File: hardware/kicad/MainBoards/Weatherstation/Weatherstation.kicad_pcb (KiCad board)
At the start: 2 copper layers, 113 x 93 mm, 37 parts, among them J1 Conn_02x07_Odd_Even, U1 ORingPower_Module, U2 24LC32, U3 ESP32-DevKitC

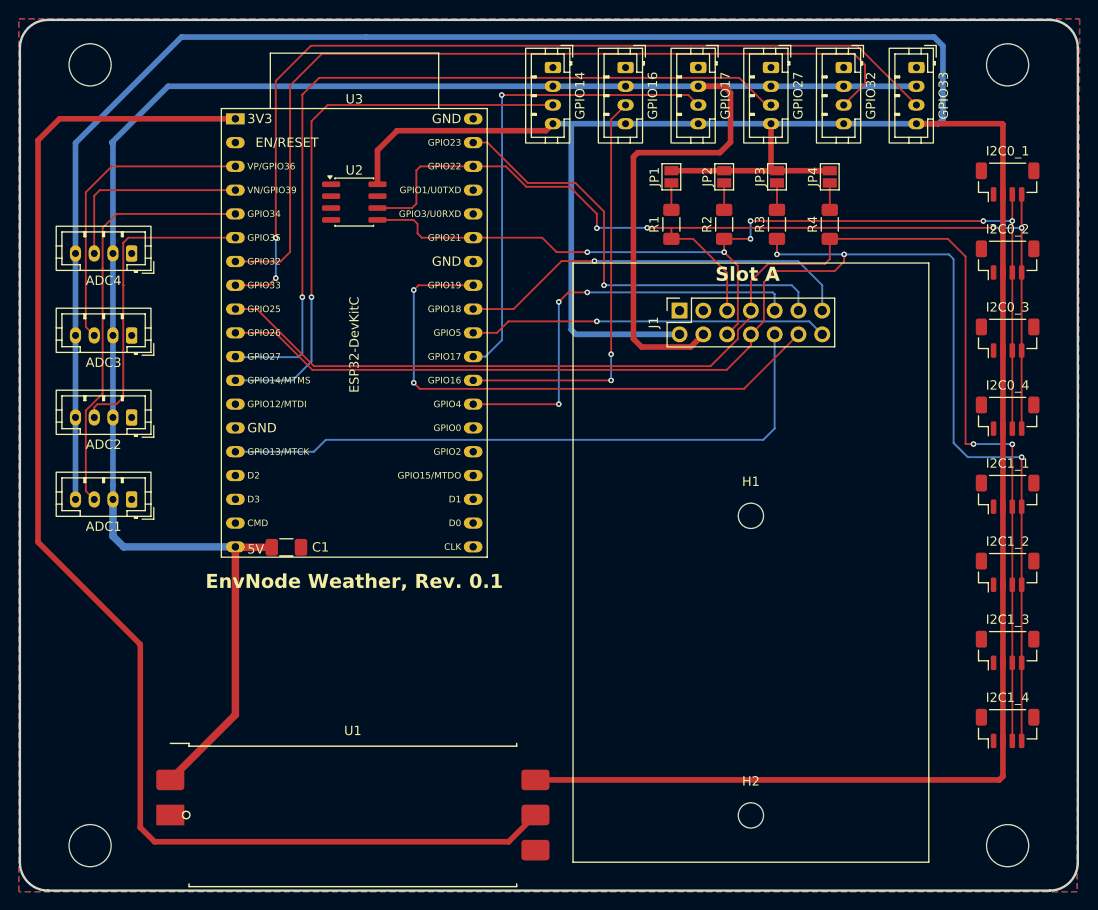
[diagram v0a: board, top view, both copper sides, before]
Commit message: hardware(weather): swap slot GPIO4 with GPIO33 for analog input
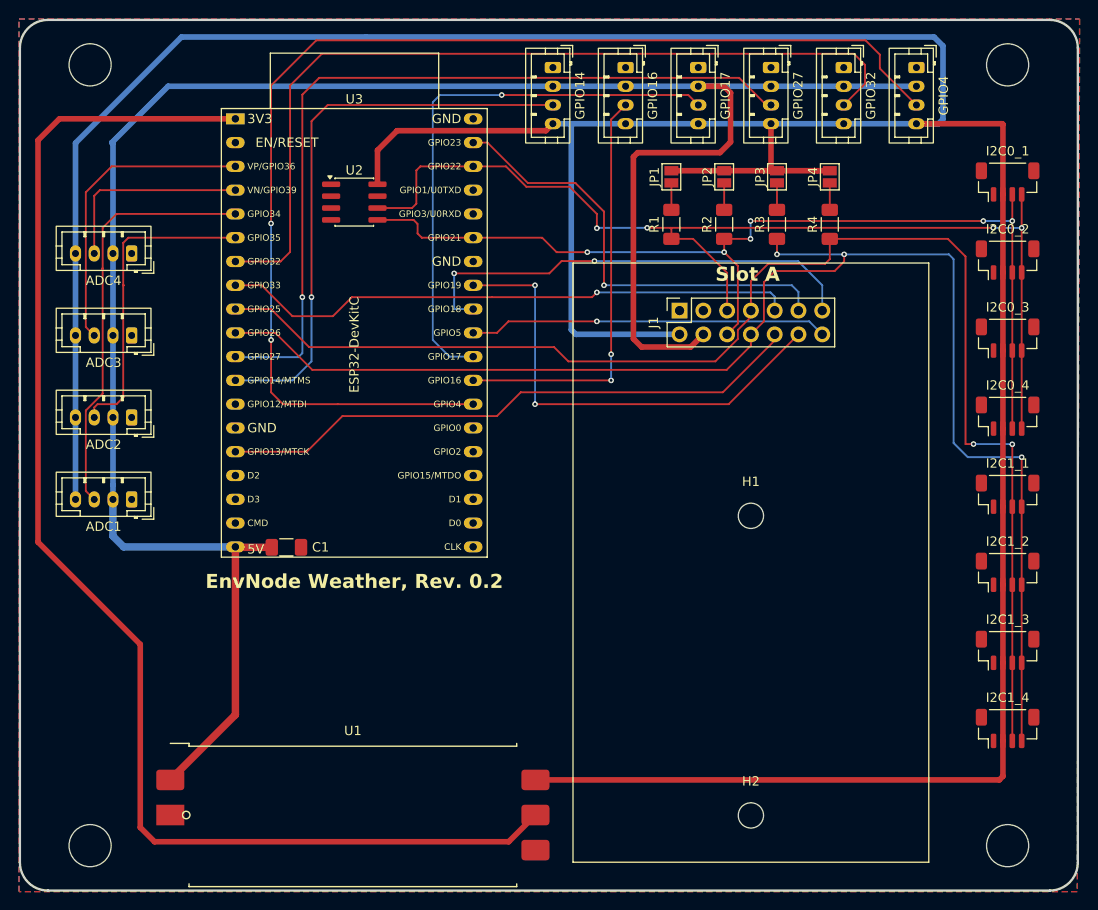
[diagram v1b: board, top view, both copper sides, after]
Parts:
- renumbered GPIO33 to GPIO4
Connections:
- GPIO4 pad 3: GPIO33 -> GPIO4
- J1 pad 9: GPIO4 -> GPIO33
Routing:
- net GPIO4: track 45.9 -> 129.5 mm, vias 3 -> 2
- net GPIO33: track 98.3 -> 62.2 mm, vias 2 -> 1
- net MISO: track 60.7 -> 51.0 mm
- net GPIO17: track 51.4 -> 59.6 mm
- net SCK: track 43.2 -> 49.5 mm, vias 1 -> 2
- net GPIO13: track 68.7 -> 63.2 mm

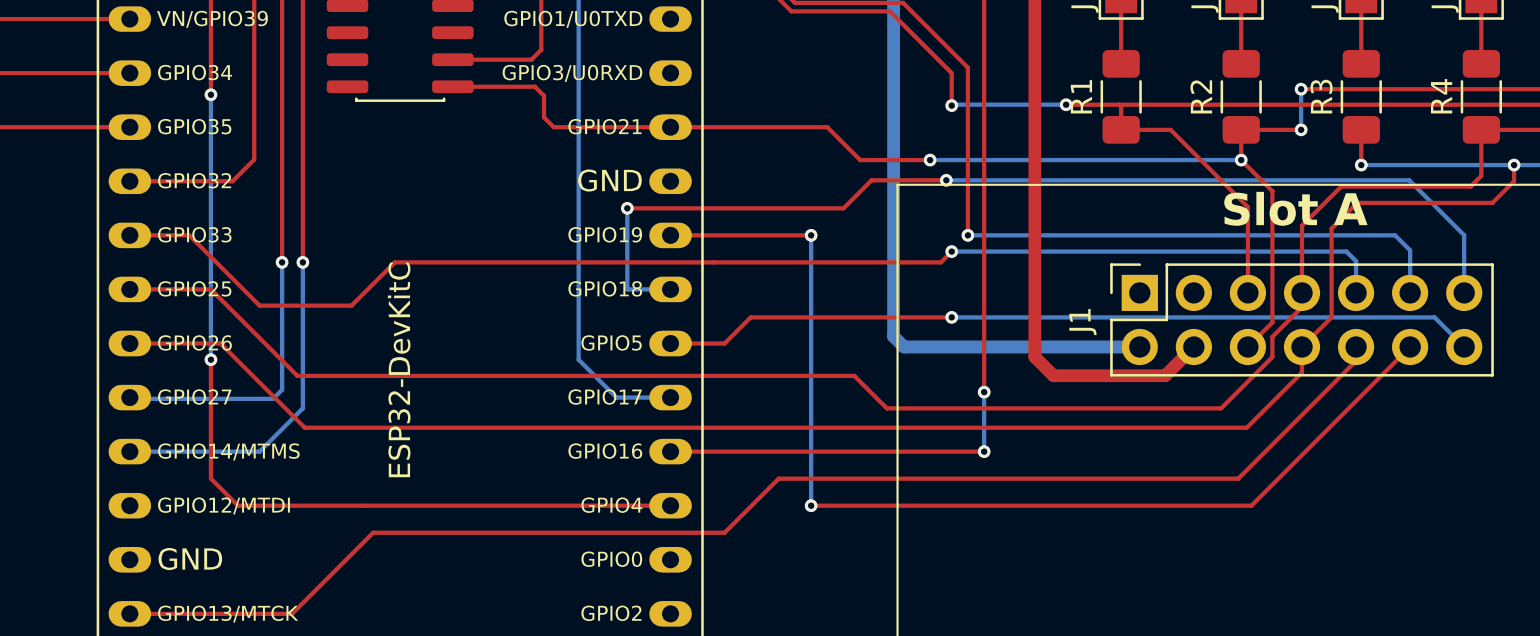
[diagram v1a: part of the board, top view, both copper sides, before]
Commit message: hardware(weather): finalize revision 0.2 with corrected module I2C0 pinout
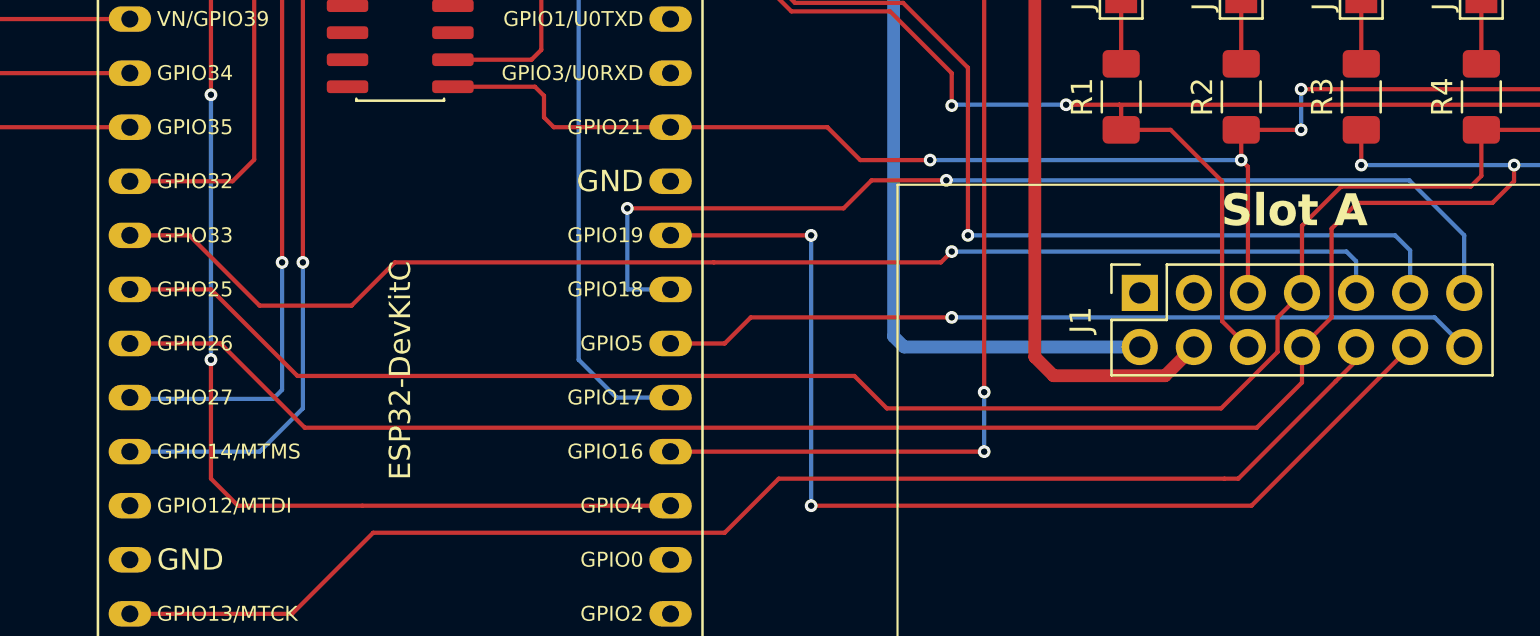
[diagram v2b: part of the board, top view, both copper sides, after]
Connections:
- J1 pad 5: I2C0_SCL -> I2C0_SDA
- J1 pad 6: I2C0_SDA -> I2C0_SCL
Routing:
- net I2C0_SDA: track 108.3 -> 104.8 mm
- net I2C0_SCL: track 114.1 -> 116.7 mm

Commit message: Document connector references and compatible PCB silkscreen revisions
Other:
- board text added: "GND +5V GPIO 3.3V"
- board text added: "GND 3V3 SDA0 SCL0"
- board text added: "GND 3V3 SDA1 SCL1"
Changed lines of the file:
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@@
 	(title_block
 		(title "EnvNode Weather")
-		(date "2026-09-28")
-		(rev "0.2")
+		(date "2026-10-18")
+		(rev "0.2.1")
 	)
 	(layers
@@
 	)
 	(footprint "Connector_JST:JST_PH_B4B-PH-K_1x04_P2.00mm_Vertical"
+		(locked yes)
 		(layer "F.Cu")
 		(at 68.17 101.35925 180)
@@
 	)
 	(footprint "Connector_JST:JST_SH_BM04B-SRSS-TB_1x04-1MP_P1.00mm_Vertical"
+		(locked yes)
 		(layer "F.Cu")
 		(at 161.73 67.455)
@@
 	)
 	(footprint "Connector_JST:JST_SH_BM04B-SRSS-TB_1x04-1MP_P1.00mm_Vertical"
+		(locked yes)
 		(layer "F.Cu")
 		(at 161.73 125.825)
@@
 		(layer "Edge.Cuts")
 	)
+	(gr_text "GND\n3V3\nSDA0\nSCL0"
+		(at 163.55245 63.17 90)
+		(layer "F.SilkS")
+		(effects
+			(font
+				(size 0.6 0.6)
+				(thickness 0.1)
+			)
+			(justify left bottom)
+		)
+	)
+	(gr_text "GND\n3V3\nSDA1\nSCL1"
+		(at 163.55245 130.8 90)
+		(layer "F.SilkS")
+		(effects
+			(font
+				(size 0.6 0.6)
+				(thickness 0.1)
+			)
+			(justify left bottom)
+		)
+	)
+	(gr_text "GND\n+5V \nGPIO\n3.3V"
+		(at 61.242109 104.71 270)
+		(layer "F.SilkS")
+		(effects
+			(font
+				(size 1.3 1.3)
+				(thickness 0.2)
+			)
+			(justify left bottom)
+		)
+	)
 	(gr_text "Slot A"
 		(locked yes)
@@
 		)
 	)
-	(group "EnvNode_Module_Connector_MainBoard"
-		(lib_id "EnvNodeDesignBlocks:EnvNode_Module_Connector_MainBoard")
-		(members "027ffce4-d752-4a7c-a46d-3b11464bb51f" "2b6a1482-f744-4401-8be8-0d3d1b676da9"
-			"4e311b5b-da68-4aa1-bb85-d9253eee2e99" "643bc130-a111-4a43-8968-95669593c117"
-			"6fa8bc57-97a8-4f35-979e-51c8c3505f15" "c3056185-6b0b-43f6-9d0d-466c7b58b56a"
-		)
-	)

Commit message: Update Mini to 0.9.0 and Weatherstation to 0.3.0
Add TP1 test reference connections isolated through D1/D2 from GND and +3V3_SYS. Replace I2C solder jumpers with removable pull-up jumpers and add C2 for local EEPROM supply decoupling.

Update schematics, PCB layouts, revision markings and KiCad project settings to match the documented hardware revisions.
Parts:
- removed JP1, JP2, JP3, JP4: Open, Jumper:SolderJumper-2_P1.3mm_Open_Pad1.0x1.5mm
- added C2: 100nF, Capacitor_SMD:C_1206_3216Metric_Pad1.33x1.80mm_HandSolder, F.Cu at (96.0, 65.4)
- added D1: 1N4148, Diode_SMD:D_1206_3216Metric_Pad1.42x1.75mm_HandSolder, F.Cu at (67.5, 116.6)
- added D2: 1N4148, Diode_SMD:D_1206_3216Metric_Pad1.42x1.75mm_HandSolder, F.Cu at (62.9, 116.6)
- added J2: Conn_01x02_Pin, Connector_PinHeader_2.54mm:PinHeader_1x02_P2.54mm_Vertical, F.Cu at (119.6, 68.2)
- added J3: Conn_01x02_Pin, Connector_PinHeader_2.54mm:PinHeader_1x02_P2.54mm_Vertical, F.Cu at (119.6, 73.8)
- added J4: Conn_01x02_Pin, Connector_PinHeader_2.54mm:PinHeader_1x02_P2.54mm_Vertical, F.Cu at (151.6, 73.8)
- added J5: Conn_01x02_Pin, Connector_PinHeader_2.54mm:PinHeader_1x02_P2.54mm_Vertical, F.Cu at (151.6, 68.2)
- added TP1: Conn_01x02_Pin, Connector_JST:JST_PH_B2B-PH-K_1x02_P2.00mm_Vertical, F.Cu at (66.2, 124.0)
- moved R3 7.50 mm to (144.4, 73.8), turned to 0 degrees
- moved R2 7.38 mm to (124.3, 73.8), turned to 0 degrees
- moved R4 4.12 mm to (144.3, 68.2), turned to 0 degrees
- moved R1 3.99 mm to (124.3, 68.3), turned to 180 degrees
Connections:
- R2 pad 1: I2C0_SDA -> Net-(J3-Pin_1)
- R2 pad 2: Net-(JP2-A) -> I2C0_SDA
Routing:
- net +3V3_SYS: track 393.8 -> 408.6 mm
- net I2C1_SDA: track 148.1 -> 161.9 mm, vias 2 -> 4
- net +5V: track 223.7 -> 214.8 mm
- net I2C1_SCL: track 154.4 -> 146.8 mm, vias 3 -> 1
- net I2C0_SDA: track 104.8 -> 111.9 mm, vias 6 -> 3
- net Net-(D2-K): track 0.00 -> 6.51 mm
- net Net-(D1-K): track 0.00 -> 6.51 mm
- net Net-(J3-Pin_1): track 0.00 -> 3.15 mm
- net Net-(JP2-A): track 2.88 -> 0.00 mm
- net SCK: track 49.5 -> 47.7 mm
- net I2C0_SCL: track 116.7 -> 118.2 mm
- net GPIO33: track 62.2 -> 61.5 mm
- net GPIO16: track 44.8 -> 44.7 mm, vias 2 -> 1
- net GPIO17: vias 1 -> 0
